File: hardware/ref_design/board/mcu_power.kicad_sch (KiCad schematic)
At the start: 19 parts

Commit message: Reference schematic: hand-laid blocks with real wiring on every sheet, drawn by a checked layout kit.
Co-Authored-By: Claude Opus 5.5 <noreply@anthropic.com>
Claude-Session: https://claude.ai/code/session_01NxPKqL46d94oRzrtCbFjri
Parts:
- added TP9: +1V1, TestPoint:TestPoint_Pad_D1.0mm, symbol Connector:TestPoint
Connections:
- net +1V1: now also TP9.1
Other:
- note added: "+1V1"
- note added: "+3V3"
- note added: "+3V3 decoupling: IOVDD, ADC_AVDD, USB_OTP_VDD, QSPI_IOVDD (100 nF each), bulk C23"
- note added: "4.7 uF at the regulator's input and output, and L2 (a polarity-marked 3.3 uH inductor, fit as drawn)."
- note added: "Core 1.1 V switcher: input, AVDD filter, inductor, output"
- note added: "DVDD decoupling (+1V1)"
- note added: "PWR_FLAG"
- note added: "RP2354B supply, as in Raspberry Pi's minimal design: 100 nF at every IOVDD, DVDD, ADC, OTP and QSPI pin,"
- note added: "VREG_VIN"
- note removed: "RP2354B supply, as in Raspberry Pi's minimal design: 100 nF at every IOVDD, DVDD, ADC, OTP and QSPI"
- note removed: "pin, 4.7 uF at the regulator's input and output, and L2 (a polarity-marked 3.3 uH inductor, fit as drawn)."

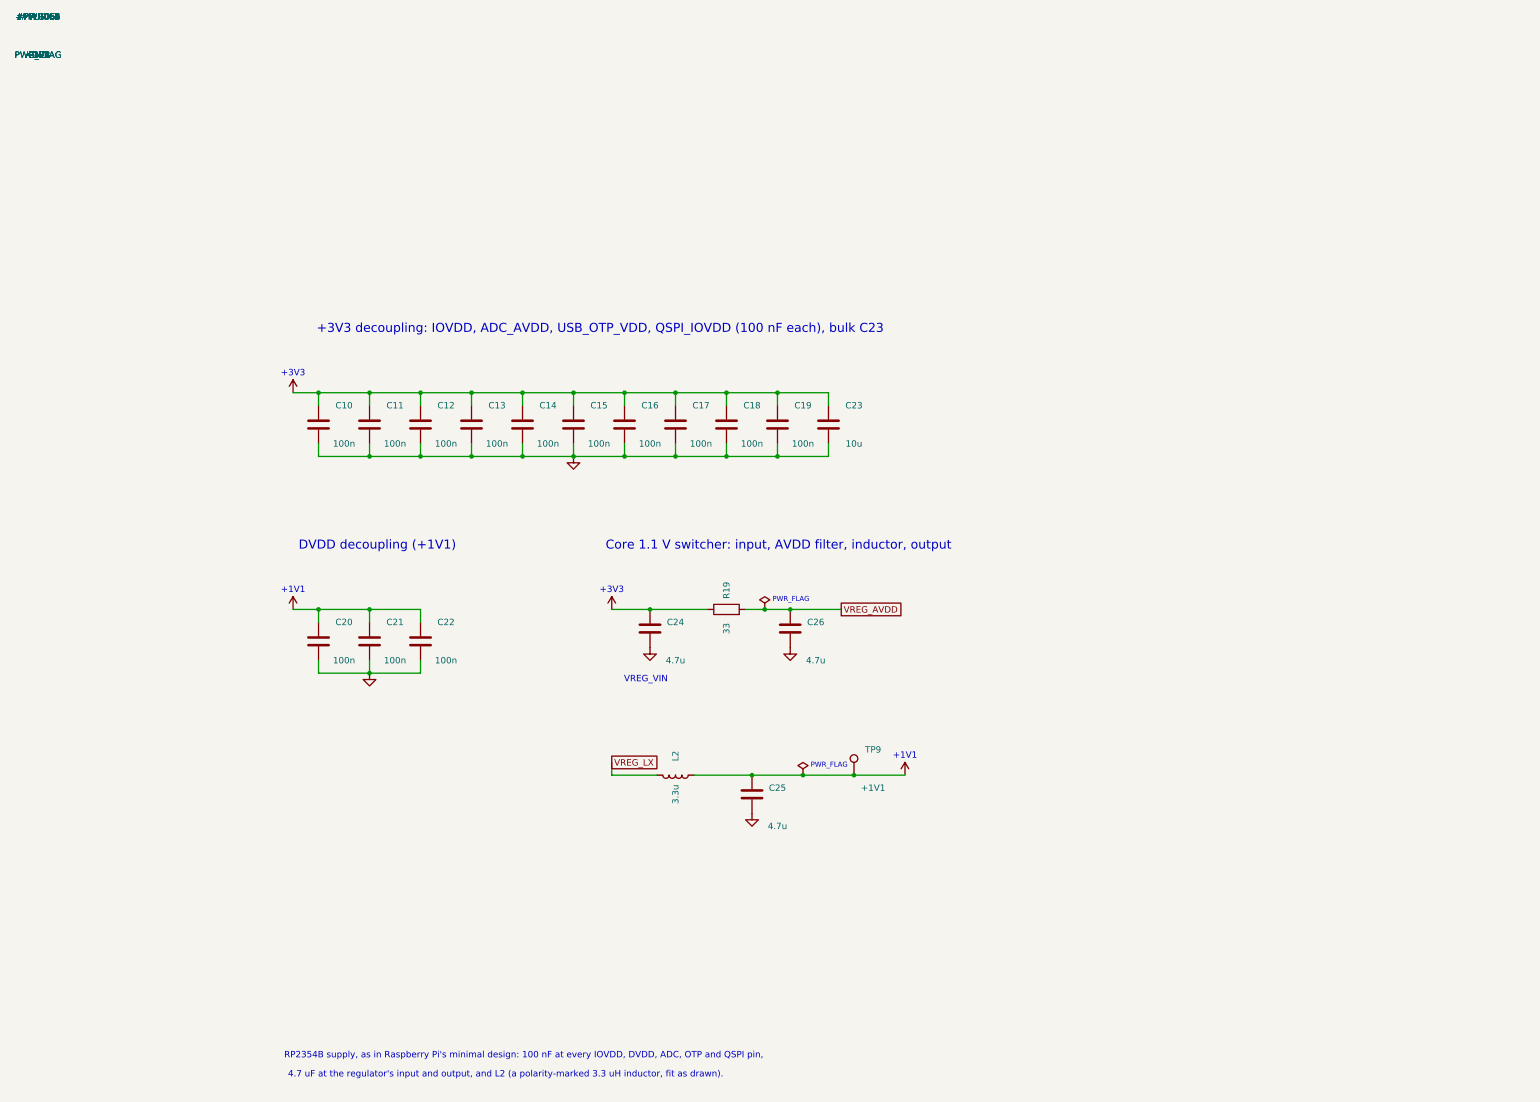
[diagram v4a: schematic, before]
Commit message: Reference schematic: written directly in KiCad 10's format and cleaned up sheet by sheet
tools/schwrite.py writes each sheet whole (library symbols flattened as KiCad caches
them, stable UUIDs, round-trip checked against KiCad's writer) instead of Konnect,
which couldn't hide a power symbol's #PWR reference or place a field: those were the
fields parked at every page's top-left. Power rails are KiCad's own symbols showing
their name; the transistors and the MCU use their real KiCad symbols; global labels
point the way their wire runs. Sheets: U3's CE wired to the latch, the ESD array on
D+/D-, the USB resistors and crystal wired to the RP2354B, J7's BOOTSEL pad wired to
its button, TP7/TP8 moved onto their nets' sheets, the FM8002A symbol widened so its
pin names clear. ERC 0, netlist check PASS (same parts, values, footprints and
connectivity; LS_GATE and AMP_SHDN are now sheet-local).

tools/sync_pcb.py brings the routed board in line without re-routing (symbol links,
fields, the two renamed nets, no-connect pads on their unconnected-(...) nets, which
KiCad's parity check expects); build_pcb.py gives no-connect pads the same nets
(copper unchanged). check_pcb PASS: 0 unconnected, 0 parity issues.

Co-Authored-By: Claude Opus 5.5 <noreply@anthropic.com>
Claude-Session: https://claude.ai/code/session_01Y3mFMxLYqNeyyedvbYuRwX
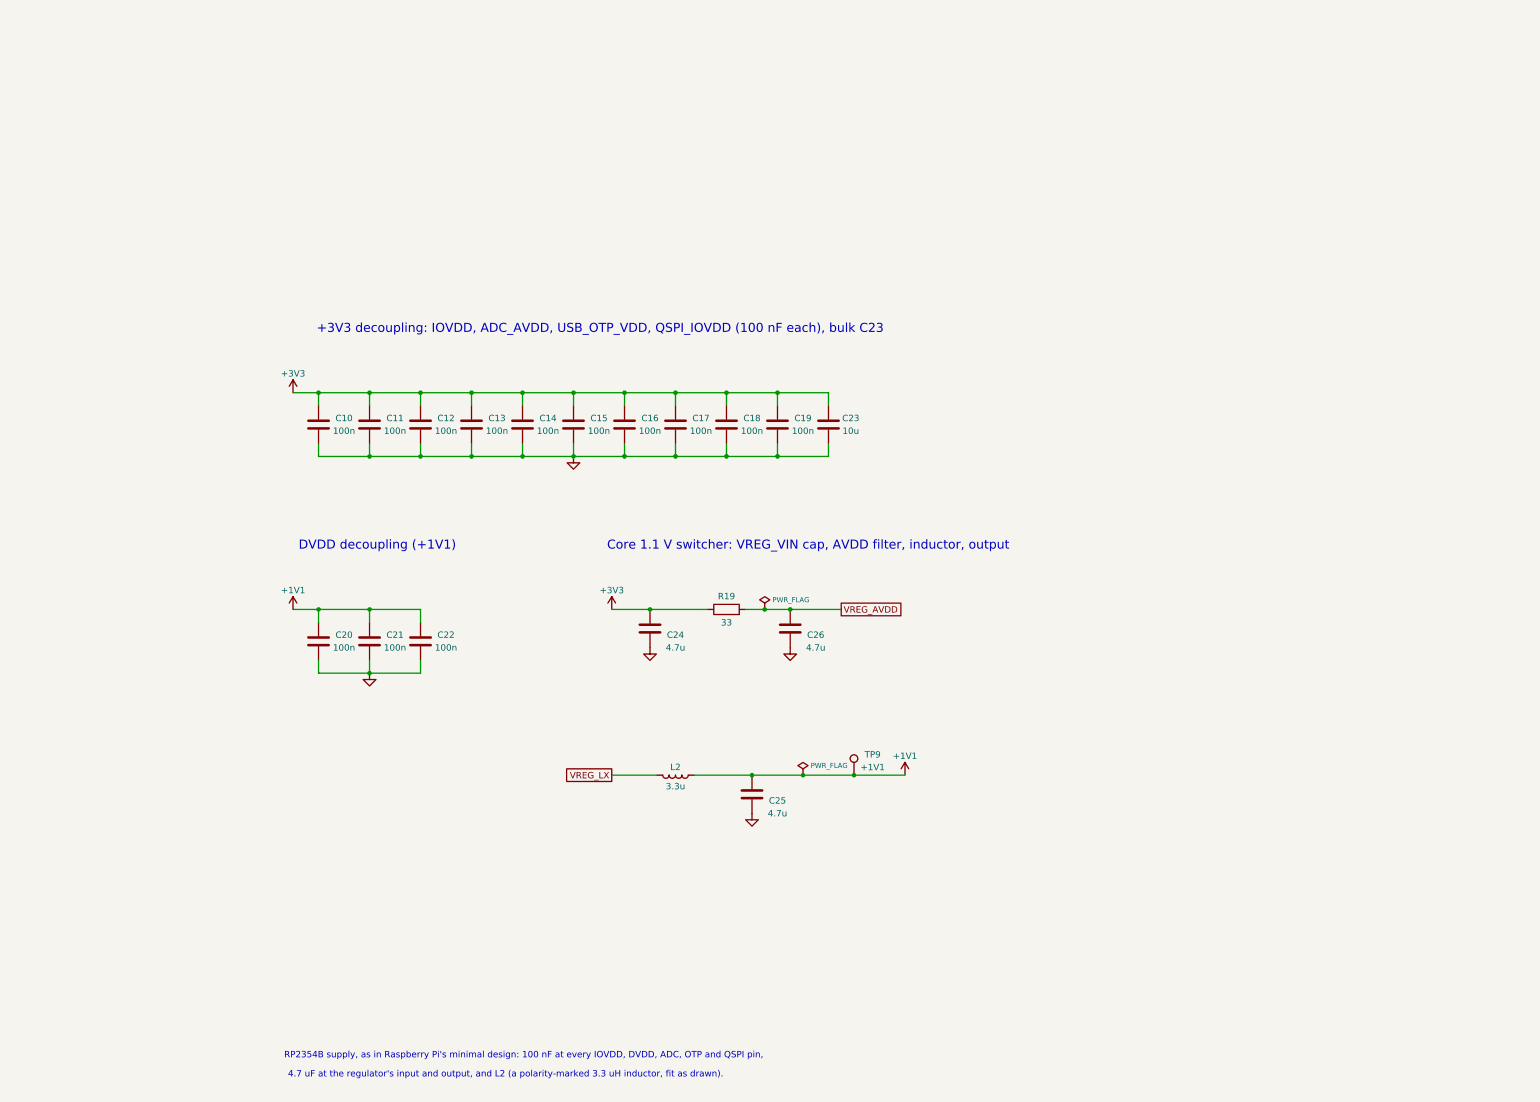
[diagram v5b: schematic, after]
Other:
- note added: "Core 1.1 V switcher: VREG_VIN cap, AVDD filter, inductor, output"
- note removed: "+1V1"
- note removed: "+3V3"
- note removed: "Core 1.1 V switcher: input, AVDD filter, inductor, output"
- note removed: "PWR_FLAG"
- note removed: "VREG_VIN"
- company: (none) -> Two-player handheld: reference design (REF-A)
- title: (none) -> RP2354B supply: decoupling and core regulator
